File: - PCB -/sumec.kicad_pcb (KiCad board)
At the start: 2 copper layers, 95 x 73 mm, 30 parts, among them IC1 XT30U-F, SW1 SW_SPDT, SW3 SW_Push, U1 ESP32-DEVKIT-V1, U10 LD1117AV33, U11 ROB-14450, U2 VL53L0X, U3 VL53L0X, U4 VL53L0X, U5 TSOP382xx, U6 QRE1113, U7 QRE1113, U8 QRE1113, U9 QRE1113

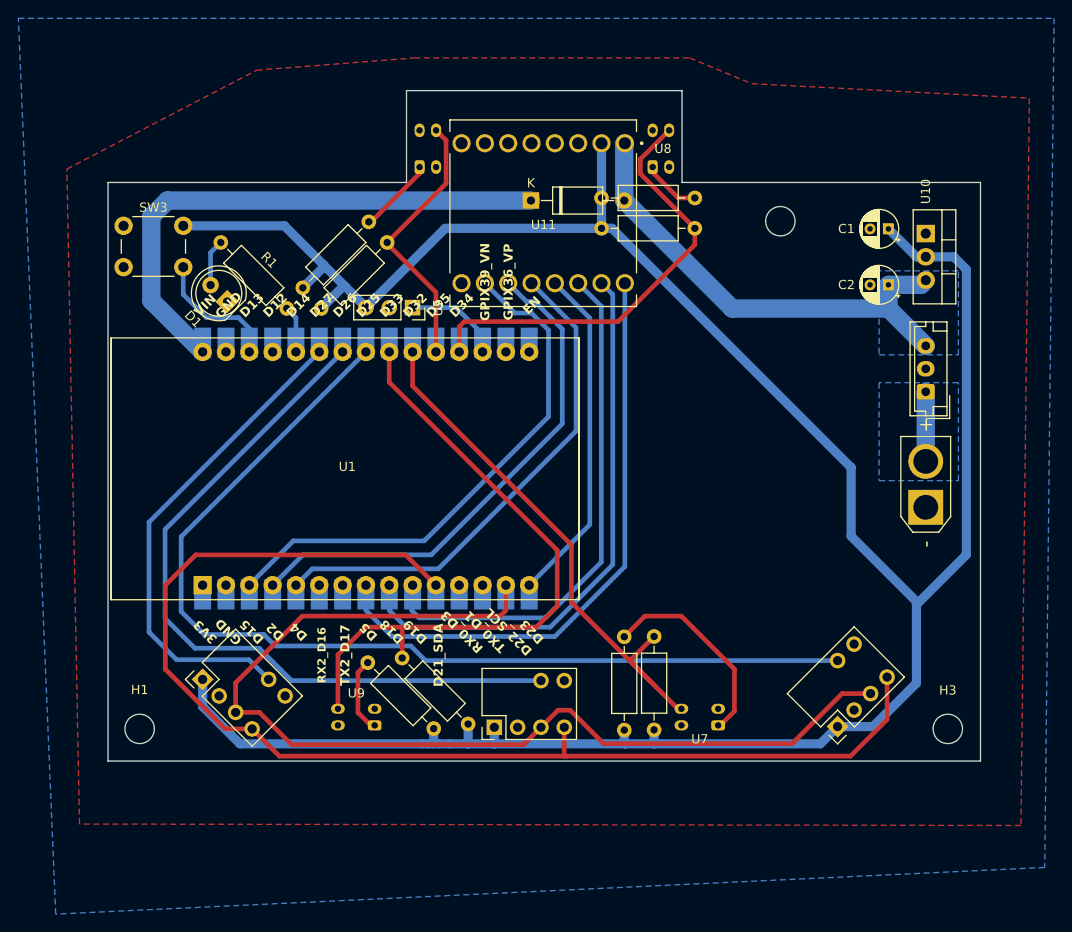
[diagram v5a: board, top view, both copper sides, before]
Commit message: PCB - pads update (riveting)
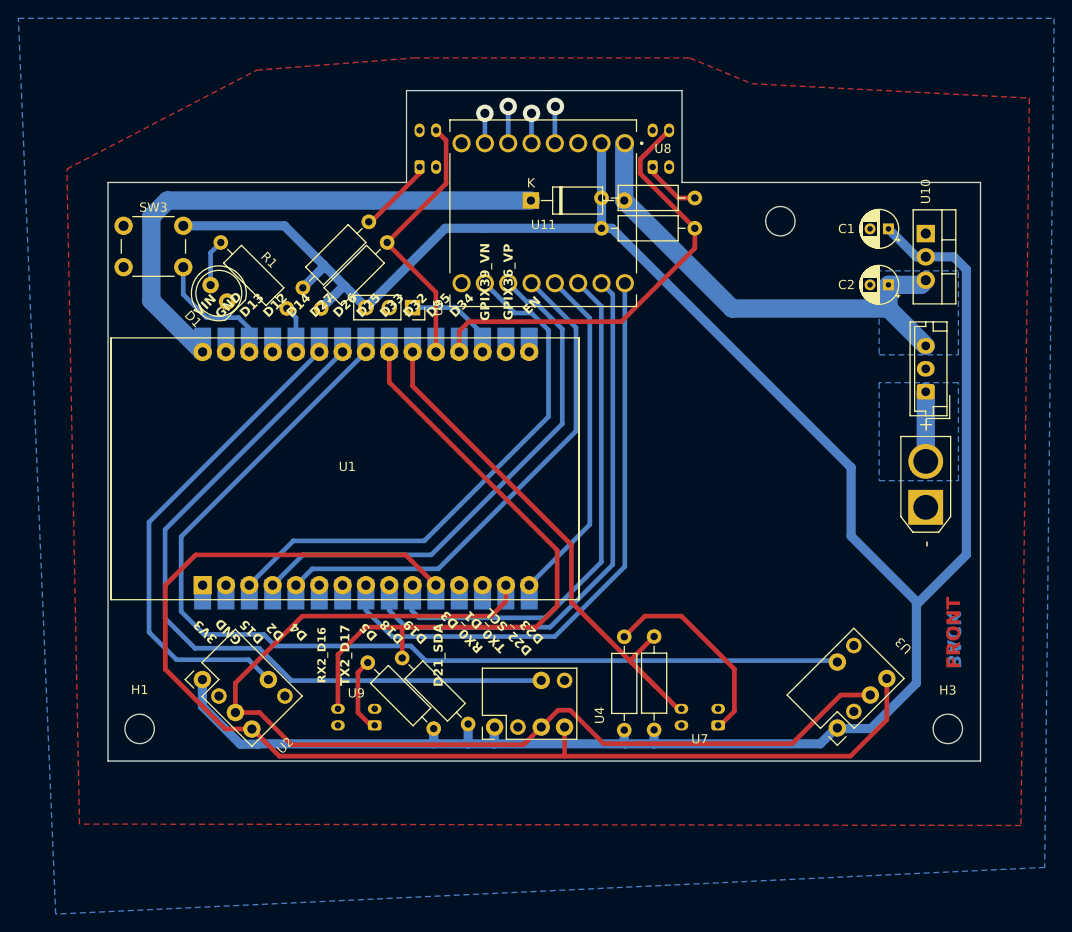
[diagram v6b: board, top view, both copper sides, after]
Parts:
- moved U3 0.16 mm to (177.0, 108.1)
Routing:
- net MOTOR 1 +: track 0.00 -> 4.28 mm, vias 0 -> 1
- net MOTOR 2 +: track 0.00 -> 4.01 mm, vias 0 -> 1
- net MOTOR 2 -: track 0.00 -> 3.26 mm, vias 0 -> 1
- net MOTOR 1 -: track 0.00 -> 3.26 mm, vias 0 -> 1
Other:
- board text added: "BACK"
- board text added: "FRONT"

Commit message: PCB - step file
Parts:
- moved D2 3.00 mm to (136.1, 57.0)
- moved R7 1.29 mm to (143.9, 64.3)
- moved R6 1.29 mm to (154.1, 61.0)
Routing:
- net +12V: track 52.5 -> 43.9 mm
- net 12V IN: track 7.58 -> 0.00 mm
- net Net-(D2-K): track 59.1 -> 60.4 mm
- net Net-(U8-A): track 5.75 -> 6.43 mm
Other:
- board text added: "SUMEC SPŠ NA PROSEKU"

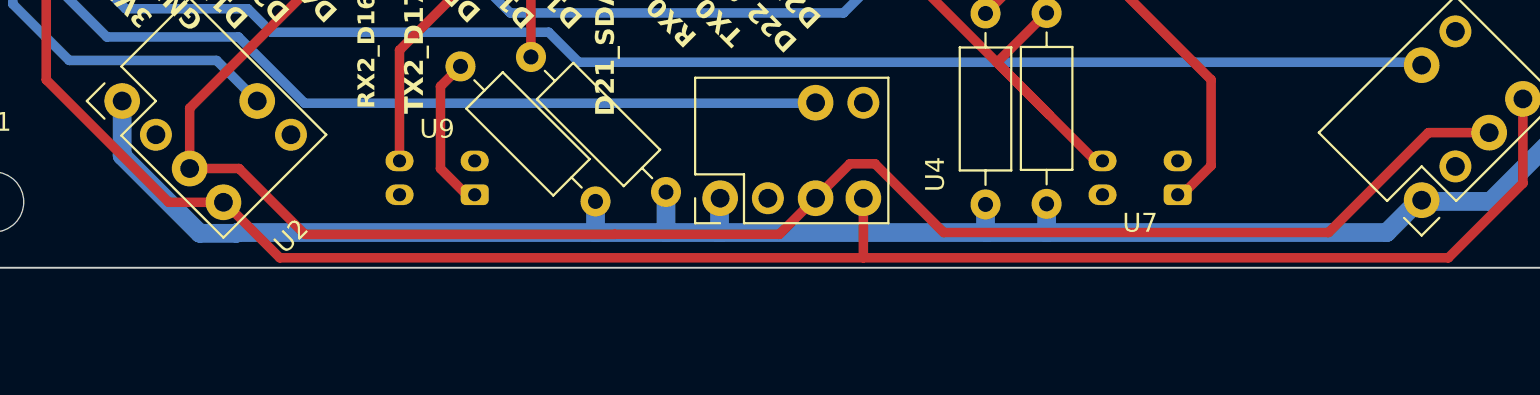
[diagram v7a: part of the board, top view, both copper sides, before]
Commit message: PCB - Board cleanup
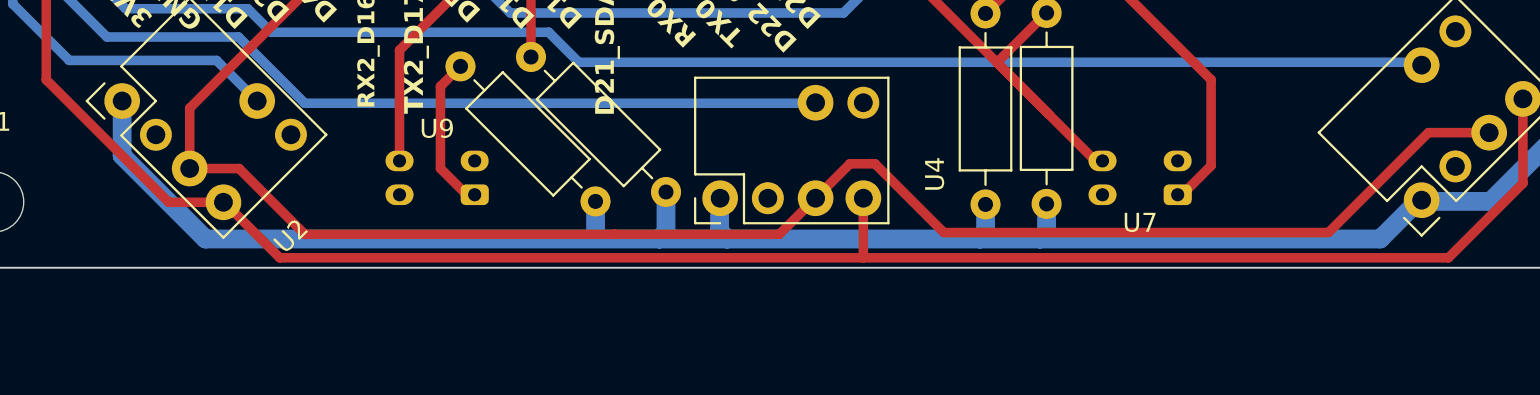
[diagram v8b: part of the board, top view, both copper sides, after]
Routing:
- net +3V3: track 276.3 -> 278.5 mm
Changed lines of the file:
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@@
     (effects (font (size 1.5 1.5) (thickness 0.3) bold) (justify left bottom mirror))
   )
+  (segment (start 149.146 119.47) (end 145.96 119.47) (width 1) (layer "B.Cu") (net 1))
   (segment (start 109.24 62.72) (end 98.22 62.72) (width 1) (layer "B.Cu") (net 1))
   (segment (start 125.49 117.47) (end 125.49 119.126) (width 1) (layer "B.Cu") (net 1))
+  (segment (start 100.305795 115.037795) (end 100.305795 112.127898) (width 1) (layer "B.Cu") (net 1))
   (segment (start 183.49 67.47) (end 183.49 98.534) (width 1) (layer "B.Cu") (net 1))
-  (segment (start 167.584001 119.126) (end 149.49 119.126) (width 1) (layer "B.Cu") (net 1))
-  (segment (start 104.434051 119.166051) (end 100.305795 115.037795) (width 1) (layer "B.Cu") (net 1))
-  (segment (start 129.24 119.126) (end 106.417453 119.126) (width 1) (layer "B.Cu") (net 1))
+  (segment (start 167.240001 119.47) (end 149.146 119.47) (width 1) (layer "B.Cu") (net 1))
   (segment (start 113.49 67.22) (end 113.49 66.97) (width 1) (layer "B.Cu") (net 1))
   (segment (start 170.942 89.672) (end 170.942 96.52) (width 1) (layer "B.Cu") (net 1))
   (segment (start 170.942 96.52) (end 178.054 103.632) (width 1) (layer "B.Cu") (net 1))
   (segment (start 179.07 66.101) (end 182.121 66.101) (width 1) (layer "B.Cu") (net 1))
+  (segment (start 146.304 119.126) (end 145.96 119.47) (width 1) (layer "B.Cu") (net 1))
   (segment (start 111.24 69.47) (end 113.49 67.22) (width 1) (layer "B.Cu") (net 1))
+  (segment (start 132.5 119.47) (end 132.08 119.05) (width 1) (layer "B.Cu") (net 1))
   (segment (start 118.11 71.59) (end 115.865 69.345) (width 1) (layer "B.Cu") (net 1))
-  (segment (start 146.304 119.126) (end 132.156 119.126) (width 1) (layer "B.Cu") (net 1))
-  (segment (start 169.240001 117.47) (end 167.584001 119.126) (width 1) (layer "B.Cu") (net 1))
+  (segment (start 128.896 119.47) (end 104.738 119.47) (width 1) (layer "B.Cu") (net 1))
   (segment (start 183.49 98.534) (end 178.054 103.97) (width 1) (layer "B.Cu") (net 1))
-  (segment (start 178.054 103.97) (end 178.054 112.522) (width 1) (layer "B.Cu") (net 1))
   (segment (start 178.054 66.101) (end 175.006 63.053) (width 1) (layer "B.Cu") (net 1))
   (segment (start 143.764 64.126) (end 143.91 64.272) (width 1) (layer "B.Cu") (net 1))
   (segment (start 115.865 69.345) (end 113.49 66.97) (width 1) (layer "B.Cu") (net 1))
-  (segment (start 100.305795 115.037795) (end 100.305795 112.127898) (width 1) (layer "B.Cu") (net 1))
-  (segment (start 178.054 112.522) (end 173.106 117.47) (width 1) (layer "B.Cu") (net 1))
   (segment (start 113.24 71.72) (end 115.615 69.345) (width 1) (layer "B.Cu") (net 1))
   (segment (start 143.91 64.272) (end 145.542 64.272) (width 1) (layer "B.Cu") (net 1))
-  (segment (start 106.417453 119.126) (end 106.377402 119.166051) (width 1) (layer "B.Cu") (net 1))
+  (segment (start 145.96 119.47) (end 132.5 119.47) (width 1) (layer "B.Cu") (net 1))
   (segment (start 143.764 53.73) (end 143.764 64.126) (width 1) (layer "B.Cu") (net 1))
+  (segment (start 132.5 119.47) (end 128.896 119.47) (width 1) (layer "B.Cu") (net 1))
   (segment (start 182.121 66.101) (end 183.49 67.47) (width 1) (layer "B.Cu") (net 1))
+  (segment (start 104.738 119.47) (end 100.305795 115.037795) (width 1) (layer "B.Cu") (net 1))
   (segment (start 113.49 66.97) (end 109.24 62.72) (width 1) (layer "B.Cu") (net 1))
-  (segment (start 132.004 119.126) (end 129.24 119.126) (width 1) (layer "B.Cu") (net 1))
+  (segment (start 178.054 103.97) (end 178.054 112.522) (width 1) (layer "B.Cu") (net 1))
   (segment (start 125.466 64.272) (end 143.91 64.272) (width 1) (layer "B.Cu") (net 1))
-  (segment (start 149.49 119.126) (end 146.304 119.126) (width 1) (layer "B.Cu") (net 1))
+  (segment (start 129.24 119.126) (end 128.896 119.47) (width 1) (layer "B.Cu") (net 1))
+  (segment (start 169.240001 117.47) (end 167.240001 119.47) (width 1) (layer "B.Cu") (net 1))
+  (segment (start 178.054 112.522) (end 173.106 117.47) (width 1) (layer "B.Cu") (net 1))
   (segment (start 132.0875 119.0425) (end 132.08 119.05) (width 1) (layer "B.Cu") (net 1))
   (segment (start 178.054 103.632) (end 178.054 103.97) (width 1) (layer "B.Cu") (net 1))
   (segment (start 118.11 71.628) (end 118.11 71.59) (width 1) (layer "B.Cu") (net 1))
-  (segment (start 132.156 119.126) (end 132.08 119.05) (width 1) (layer "B.Cu") (net 1))
   (segment (start 173.106 117.47) (end 169.240001 117.47) (width 1) (layer "B.Cu") (net 1))
   (segment (start 118.11 71.628) (end 125.466 64.272) (width 1) (layer "B.Cu") (net 1))
   (segment (start 132.0875 117.325) (end 132.0875 119.0425) (width 1) (layer "B.Cu") (net 1))
-  (segment (start 106.377402 119.166051) (end 104.434051 119.166051) (width 1) (layer "B.Cu") (net 1))
   (segment (start 115.615 69.345) (end 115.865 69.345) (width 1) (layer "B.Cu") (net 1))
-  (segment (start 132.08 119.05) (end 132.004 119.126) (width 1) (layer "B.Cu") (net 1))
   (segment (start 129.24 116.97) (end 129.24 119.126) (width 1) (layer "B.Cu") (net 1))
   (segment (start 145.542 64.272) (end 170.942 89.672) (width 1) (layer "B.Cu") (net 1))
@@
   (segment (start 149.49 117.602) (end 149.49 119.126) (width 1) (layer "B.Cu") (net 1))
   (segment (start 146.24 119.062) (end 146.304 119.126) (width 1) (layer "B.Cu") (net 1))
+  (segment (start 149.49 119.126) (end 149.146 119.47) (width 1) (layer "B.Cu") (net 1))
   (segment (start 146.24 59.97) (end 157.999 71.729) (width 2) (layer "B.Cu") (net 3))
   (segment (start 157.999 71.729) (end 178.99 71.729) (width 2) (layer "B.Cu") (net 3))
